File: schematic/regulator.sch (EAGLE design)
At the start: 29 parts, among them J1 COMM, J2 STOP_LIGHT, J3 ON/OFF, J4 BATTERY, J5 DRIVER, J6 DRIVER POWER, Q1 NMOSFETSOT23, Q2 NMOSFETSOT23, Q3 NMOSFETSOT23, Q4 IRFR3607PBF

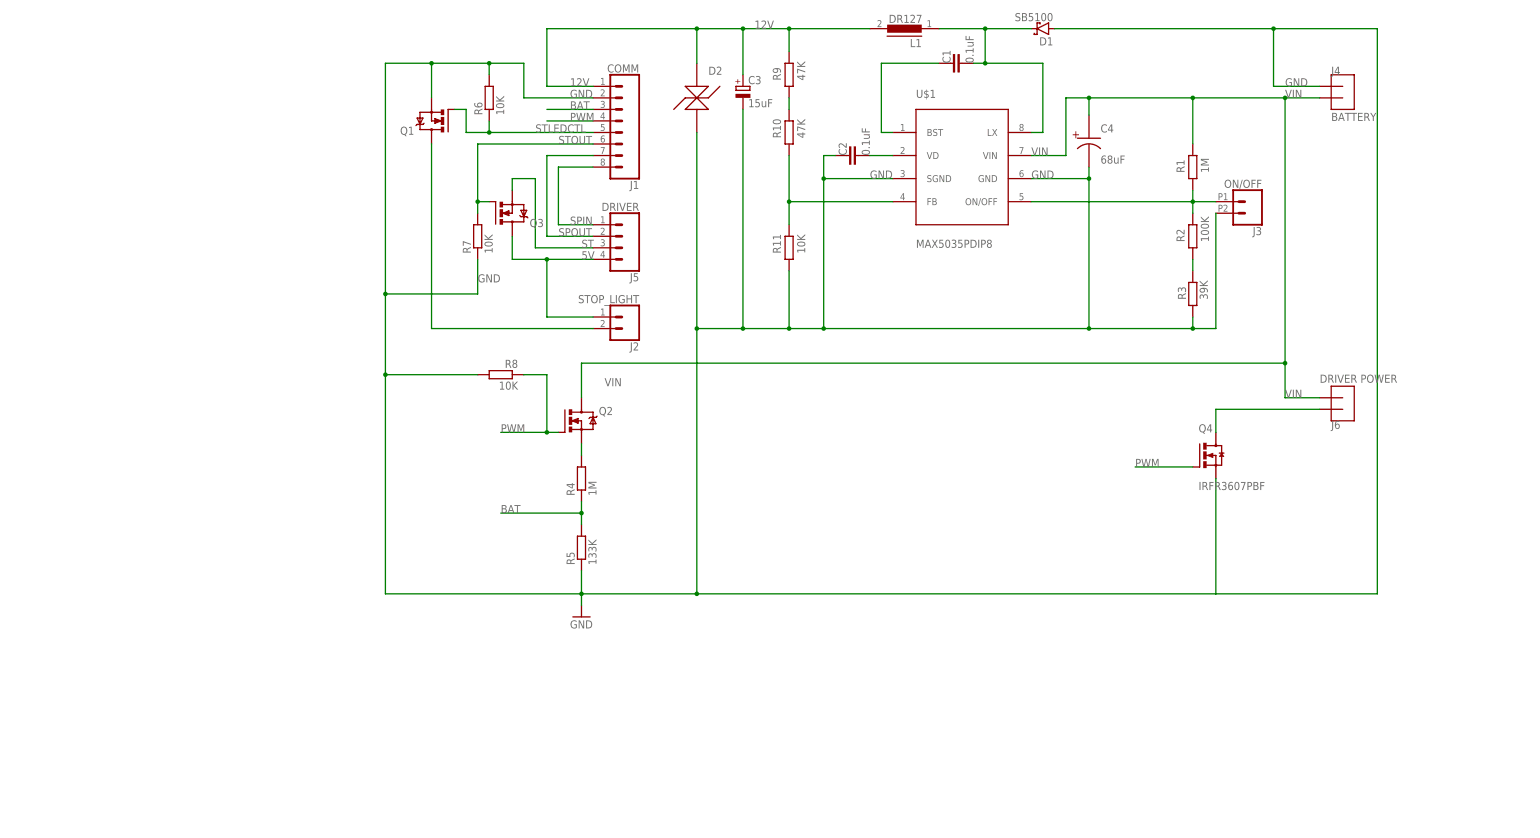
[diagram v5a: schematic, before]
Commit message: Replace low-side BLDC driver switch by high-side switch
- Rearrange elements on regulator schematics
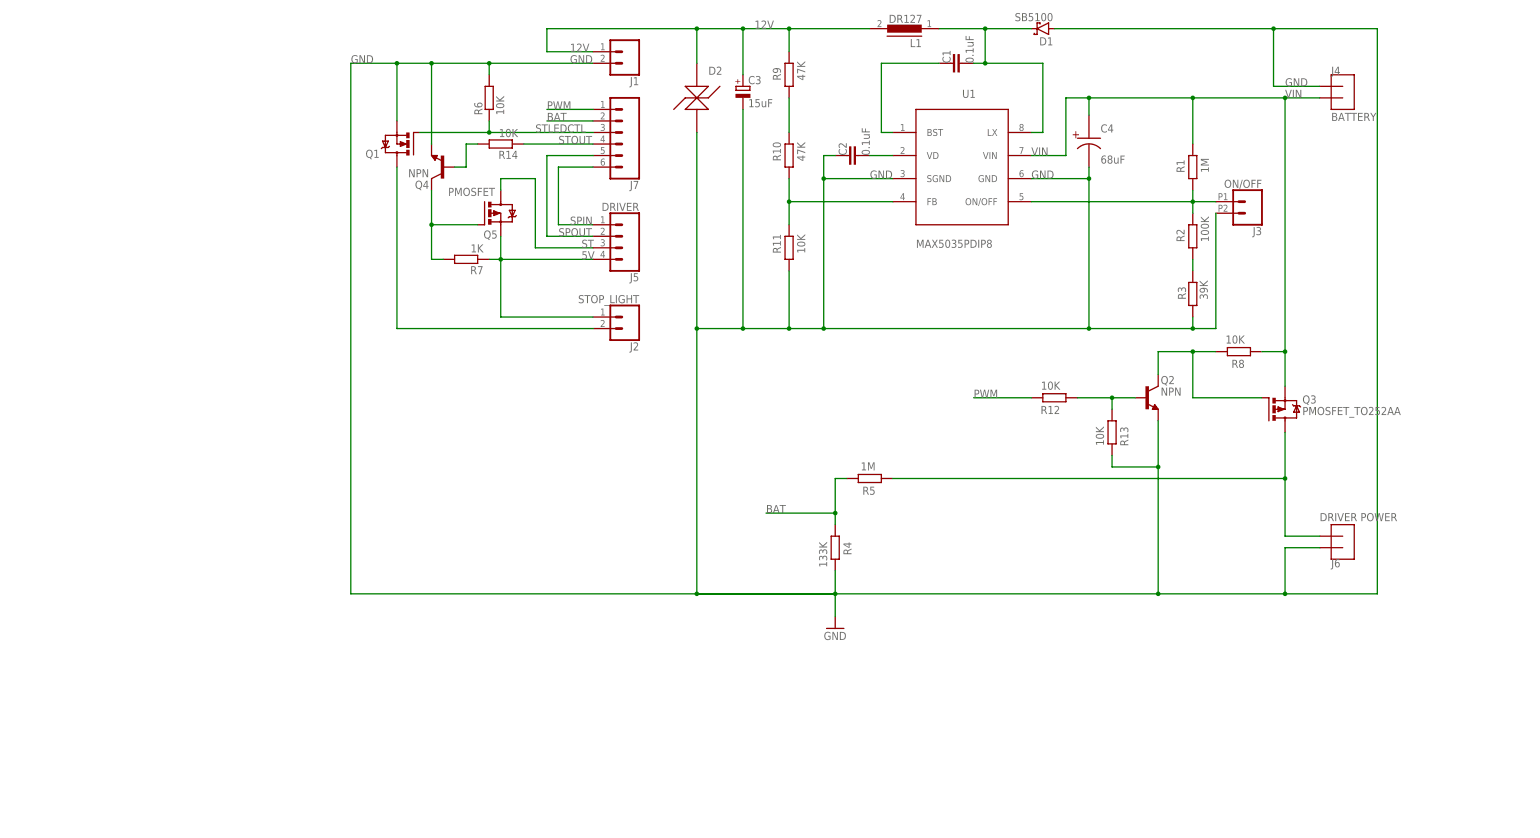
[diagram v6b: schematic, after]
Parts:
- added J7: (no value), SparkFun-Connectors:CONN_06LONGPADS
- added Q5: PMOSFET, Transistor:PMOSFET_SOT23
- added R12, R13, R14: 10K, eagle-ltspice:RR1206
- J1: value COMM -> (none); device SparkFun-Connectors:CONN_08LONGPADS -> SparkFun-Connectors:CONN_02PTH3
- Q2: value NMOSFETSOT23 -> NPN; device Transistor:NMOSFETSOT23 -> Transistor:NPN_TO92
- Q3: value NMOSFETSOT23 -> PMOSFET_TO252AA; device Transistor:NMOSFETSOT23 -> Transistor:PMOSFET_TO252AA
- Q4: value IRFR3607PBF -> NPN; device Transistor:FQD13N06LTM -> Transistor:NPN_SOT23
- R4: value 1M -> 133K; device eagle-ltspice:RR1210 -> eagle-ltspice:RR1206
- R5: value 133K -> 1M; device eagle-ltspice:RR1210 -> eagle-ltspice:RR1206
- R7: value 10K -> 1K
- renumbered U$1 to U1
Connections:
- removed net P$1: J6.P$1, Q4.D
- new net N$10: Q2.B, R12.2, R13.2
- new net N$11: Q4.C, Q5.G, R7.2
- new net N$12: Q4.B, R14.2
- new net P$2: J6.P$2, Q3.D, R5.2
- net 5V: now also Q5.S, R7.1; no longer Q3.D
- net BAT: now also J7.2, R4.2, R5.1; no longer J1.3, R4.1, R5.2
- net GND: now also J6.P$1, Q2.E, Q4.E, R13.1, R4.1; no longer Q4.S, R5.1, R7.1, R8.2
- net N$8: now also Q2.C, Q3.G, R8.1; no longer Q2.S, R4.2
- net PWM: now also J7.1, R12.1; no longer J1.4, Q2.G, Q4.G, R8.1
- net SPIN: now also J7.6; no longer J1.8
- net SPOUT: now also J7.5; no longer J1.7
- net ST: now also Q5.D; no longer Q3.S
- net STLEDCTL: now also J7.3; no longer J1.5
- net STOUT: now also J7.4, R14.1; no longer J1.6, Q3.G, R7.2
- net VIN: now also Q3.S, R8.2; no longer J6.P$2, Q2.D
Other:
- moved on the sheet: J6, Q1, R10, R4, R5, R7, R8

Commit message: Remove high-side switch for driver
- Keep driver alway on for now
- Add mosfet switched for speed and throttle
- Align break work
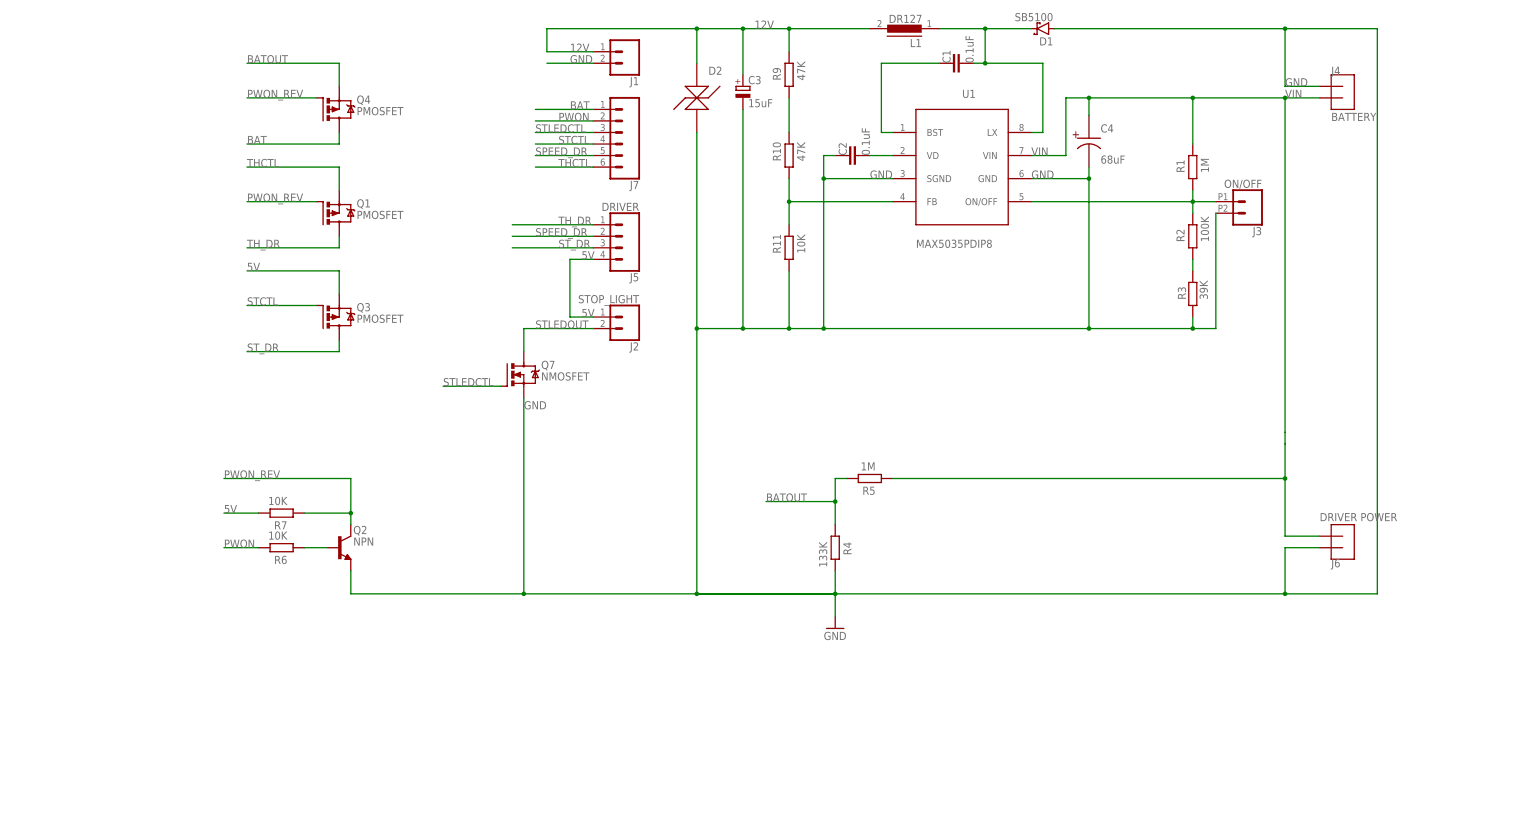
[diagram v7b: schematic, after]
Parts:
- removed Q5: PMOSFET, Transistor:PMOSFET_SOT23
- removed R12, R13, R14, R8: 10K, eagle-ltspice:RR1206
- added Q7: NMOSFET, Transistor:NMOSFETSOT23
- Q1: value NMOSFETSOT23 -> PMOSFET; device Transistor:NMOSFETSOT23 -> Transistor:PMOSFET_SOT23
- Q2: device Transistor:NPN_TO92 -> Transistor:NPN_SOT23
- Q3: value PMOSFET_TO252AA -> PMOSFET; device Transistor:PMOSFET_TO252AA -> Transistor:PMOSFET_SOT23
- Q4: value NPN -> PMOSFET; device Transistor:NPN_SOT23 -> Transistor:PMOSFET_SOT23
- R7: value 1K -> 10K
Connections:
- net SPOUT renamed SPEED_DR
- removed net N$10: Q2.B, R12.2, R13.2
- removed net N$11: Q4.C, Q5.G, R7.2
- removed net N$12: Q4.B, R14.2
- removed net N$8: Q2.C, Q3.G, R8.1
- removed net P$2: J6.P$2, Q3.D, R5.2
- removed net PWM: J7.1, R12.1
- removed net SPIN: J5.1, J7.6
- removed net ST: J5.3, Q5.D
- removed net STOUT: J7.4, R14.1
- new net BATOUT: Q4.S, R4.2, R5.1
- new net PWON: J7.2, R6.1
- new net PWON_REV: Q1.G, Q2.C, Q4.G, R7.2
- new net STCTL: J7.4, Q3.G
- new net STLEDOUT: J2.2, Q7.D
- new net ST_DR: J5.3, Q3.D
- new net THCTL: J7.6, Q1.S
- new net TH_DR: J5.1, Q1.D
- net 5V: now also Q3.S; no longer Q5.S
- net BAT: now also J7.1, Q4.D; no longer J7.2, R4.2, R5.1
- net GND: now also Q7.S; no longer Q1.S, Q4.E, R13.1, R6.2
- net N$3: now also Q2.B, R6.2; no longer J2.2, Q1.D
- net STLEDCTL: now also Q7.G; no longer Q1.G, R6.1
- net VIN: now also J6.P$2, R5.2; no longer Q3.S, R8.2
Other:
- moved on the sheet: Q2, Q3, R6, R7

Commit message: Cosmetical updates on schematics
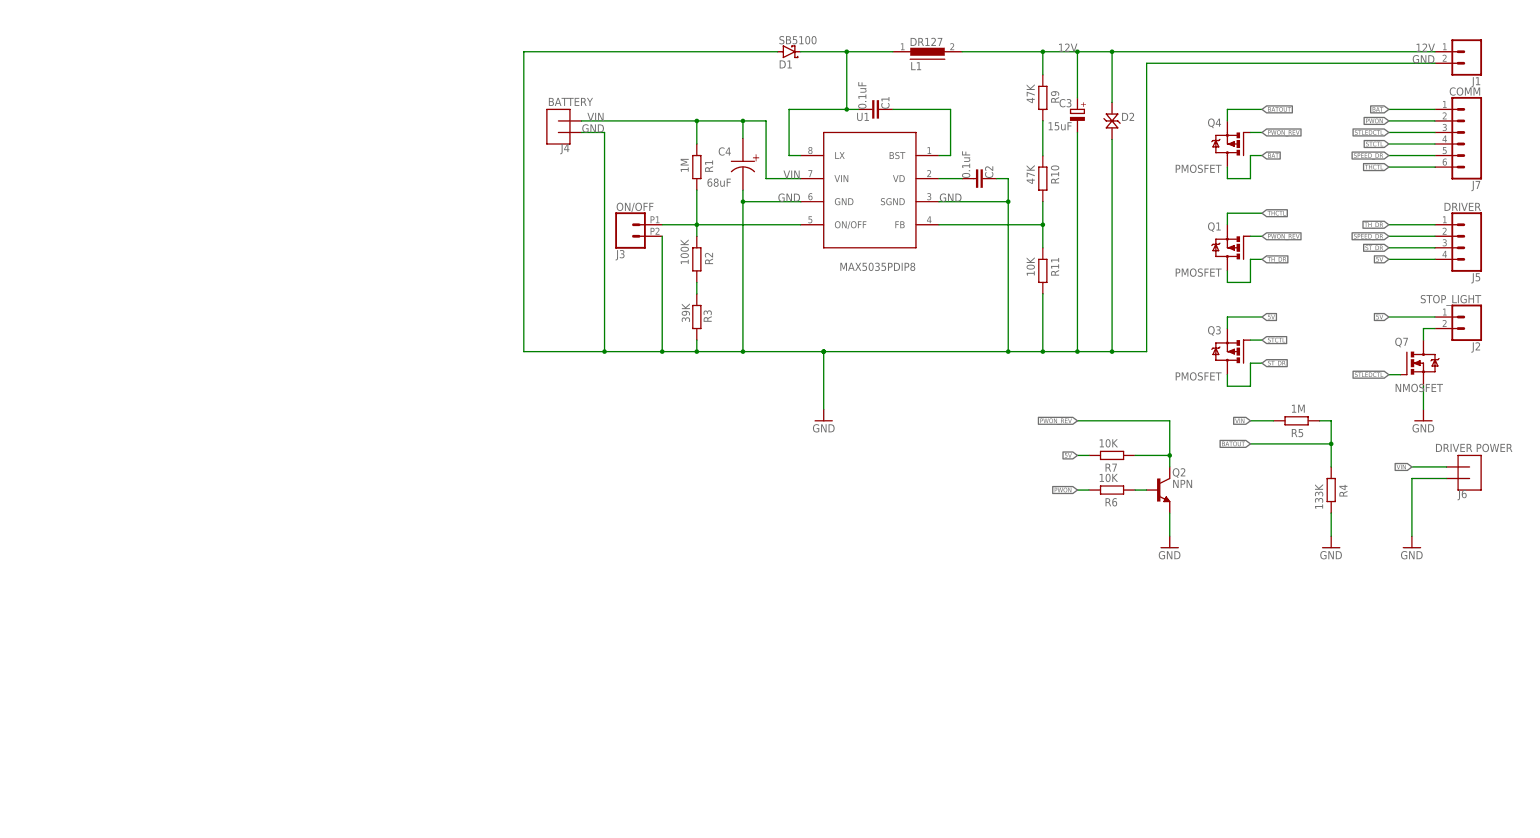
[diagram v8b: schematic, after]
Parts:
- J7: value (none) -> COMM
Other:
- moved on the sheet: C1, C2, C3, C4, D1, D2, J1, J2, J3, J4, J5, J6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
